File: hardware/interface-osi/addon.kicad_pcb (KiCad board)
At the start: 2 copper layers, 43.2 x 54 mm, 23 parts, among them J1 Conn_01x16, U1 4066, U2 74HC14

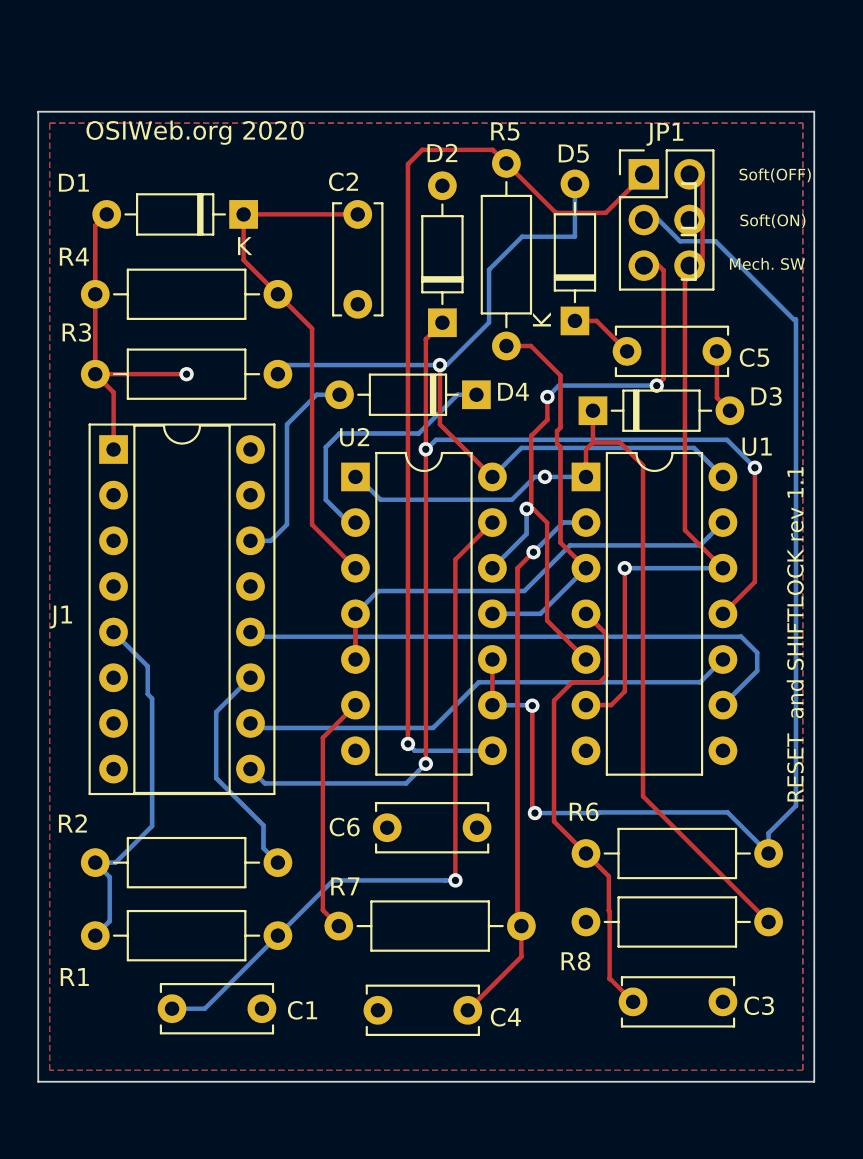
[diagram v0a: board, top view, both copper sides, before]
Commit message: OSI reset/shiftlock addon- add  mounting holes
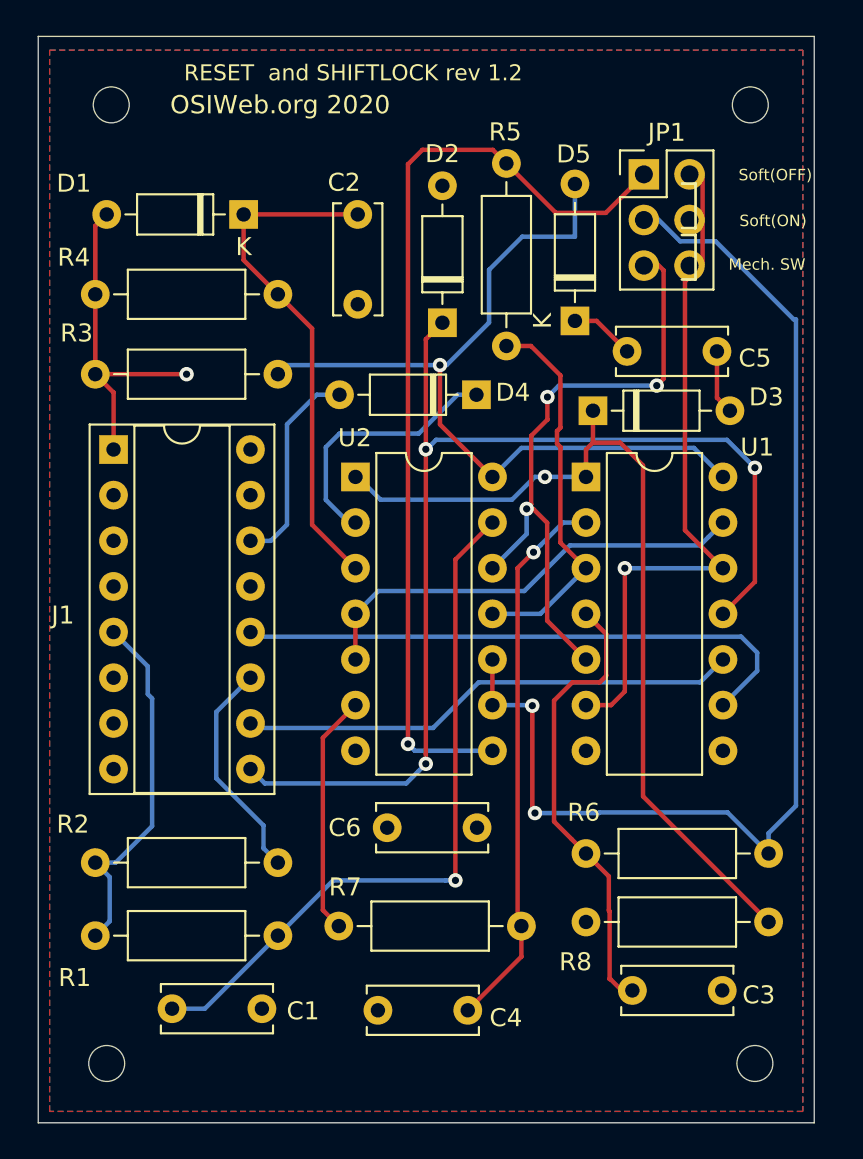
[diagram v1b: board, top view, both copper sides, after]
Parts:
- added REF**: MountingHole_2mm, MountingHole:MountingHole_2mm, F.Cu at (110.7, 42.2)
- added REF**: MountingHole_2mm, MountingHole:MountingHole_2mm, F.Cu at (110.5, 95.5)
- added REF**: MountingHole_2mm, MountingHole:MountingHole_2mm, F.Cu at (146.3, 42.2)
- added REF**: MountingHole_2mm, MountingHole:MountingHole_2mm, F.Cu at (146.6, 95.5)
- moved C3 0.64 mm to (144.7, 91.4)
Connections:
- net ~RESET renamed ~{RESET}
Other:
- board size 43.2 x 54 mm -> 43.2 x 60.5 mm
- net class Default removed
- board text added: "RESET and SHIFTLOCK rev 1.2"
- board text removed: "RESET and SHIFTLOCK rev 1.1"

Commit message: Clean up DRC errors
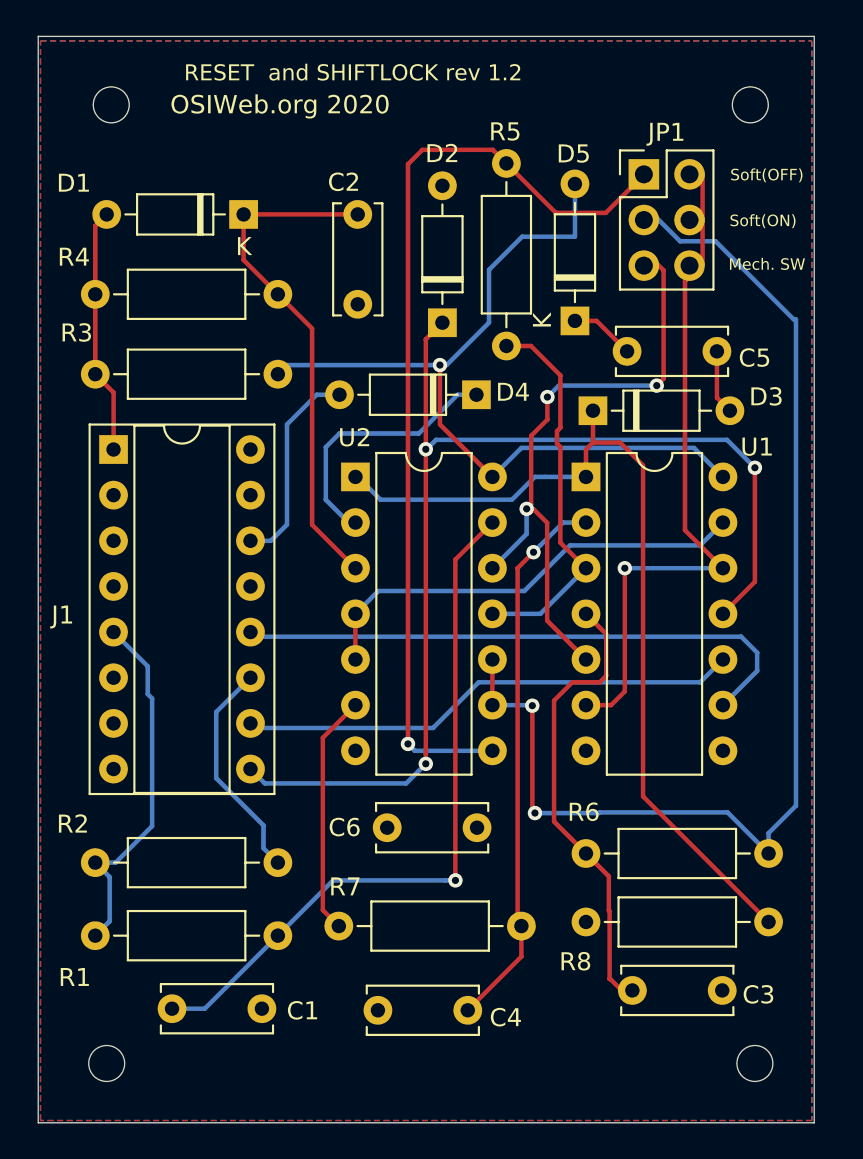
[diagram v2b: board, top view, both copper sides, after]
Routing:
- net /Break1: track 18.8 -> 13.8 mm, vias 1 -> 0
- net Net-(C3-Pad2): track 26.6 -> 26.0 mm
- net Net-(D3-Pad1): vias 1 -> 0
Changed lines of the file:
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@@
     (pad "" np_thru_hole circle (at 0 0) (size 2 2) (drill 2) (layers *.Cu *.Mask))
   )
-  (gr_line (start 142.494 49.403) (end 143.256 49.403) (layer "F.SilkS") (width 0.15))
-  (gr_line (start 142.494 49.022) (end 143.256 49.022) (layer "F.SilkS") (width 0.15))
-  (gr_line (start 142.494 46.5455) (end 143.256 46.5455) (layer "F.SilkS") (width 0.15))
-  (gr_line (start 143.256 49.022) (end 143.256 46.5455) (layer "F.SilkS") (width 0.15))
-  (gr_line (start 142.494 51.8795) (end 143.256 51.8795) (layer "F.SilkS") (width 0.15))
-  (gr_line (start 143.256 51.8795) (end 143.256 49.403) (layer "F.SilkS") (width 0.15))
   (gr_rect (start 149.86 98.806) (end 106.68 38.354) (layer "Edge.Cuts") (width 0.0508) (fill none))
-  (gr_text "Soft(ON)" (at 147.56892 48.6156) (layer "F.SilkS")
+  (gr_text "Soft(ON)" (at 147.016893 48.6156) (layer "F.SilkS")
     (effects (font (size 0.635 0.635) (thickness 0.127)))
   )
-  (gr_text "Soft(OFF)" (at 147.69592 46.06544) (layer "F.SilkS")
+  (gr_text "Soft(OFF)" (at 147.22856 46.06544) (layer "F.SilkS")
     (effects (font (size 0.635 0.635) (thickness 0.127)))
   )
@@
   (segment (start 110.871 58.166) (end 109.855 57.15) (width 0.25) (layer "F.Cu") (net 2))
   (segment (start 109.855 52.705) (end 109.855 48.895) (width 0.25) (layer "F.Cu") (net 2))
-  (segment (start 109.855 57.15) (end 114.935 57.15) (width 0.25) (layer "F.Cu") (net 2))
   (segment (start 110.871 61.341) (end 110.871 58.166) (width 0.25) (layer "F.Cu") (net 2))
   (segment (start 109.855 48.895) (end 110.49 48.26) (width 0.25) (layer "F.Cu") (net 2))
-  (via (at 114.935 57.15) (size 0.8) (drill 0.4) (layers "F.Cu" "B.Cu") (net 2))
   (segment (start 128.246598 61.327758) (end 128.246598 78.264325) (width 0.25) (layer "F.Cu") (net 3))
   (segment (start 128.246598 78.264325) (end 128.246598 78.83001) (width 0.25) (layer "F.Cu") (net 3))
@@
   (segment (start 148.844 54.102) (end 148.717 54.102) (width 0.25) (layer "B.Cu") (net 4))
   (segment (start 147.32 83.82) (end 147.32 82.68863) (width 0.25) (layer "B.Cu") (net 4))
-  (segment (start 147.32 83.82) (end 147.2565 83.7565) (width 0.25) (layer "B.Cu") (net 4))
   (segment (start 137.922 81.534) (end 145.034 81.534) (width 0.25) (layer "B.Cu") (net 4))
   (segment (start 142.39748 49.75352) (end 141.10716 48.4632) (width 0.25) (layer "B.Cu") (net 4))
@@
   (segment (start 138.285001 73.931999) (end 137.922 74.295) (width 0.25) (layer "F.Cu") (net 16))
   (segment (start 136.360001 83.020001) (end 137.16 83.82) (width 0.25) (layer "F.Cu") (net 16))
-  (segment (start 137.16 83.82) (end 137.795 83.82) (width 0.25) (layer "F.Cu") (net 16))
   (segment (start 138.285001 71.610001) (end 138.285001 73.931999) (width 0.25) (layer "F.Cu") (net 16))
   (segment (start 136.398 74.295) (end 135.382 75.311) (width 0.25) (layer "F.Cu") (net 16))
@@
   (segment (start 139.065 60.96) (end 137.541 60.96) (width 0.25) (layer "F.Cu") (net 22))
   (segment (start 140.335 62.23) (end 139.065 60.96) (width 0.25) (layer "F.Cu") (net 22))
-  (via (at 134.874 62.865) (size 0.8) (drill 0.4) (layers "F.Cu" "B.Cu") (net 22))
   (segment (start 125.73 64.135) (end 133.038315 64.135) (width 0.25) (layer "B.Cu") (net 22))
   (segment (start 133.038315 64.135) (end 134.308315 62.865) (width 0.25) (layer "B.Cu") (net 22))
@@
   (segment (start 128.0541 44.6659) (end 127.254 45.466) (width 0.25) (layer "F.Cu") (net 24))
   (segment (start 138.26236 48.17364) (end 135.4836 48.17364) (width 0.25) (layer "F.Cu") (net 24))
-  (segment (start 141.10716 45.9232) (end 140.90904 45.9232) (width 0.25) (layer "F.Cu") (net 24))
   (segment (start 131.97586 44.6659) (end 128.0541 44.6659) (width 0.25) (layer "F.Cu") (net 24))
   (segment (start 140.38072 46.05528) (end 138.26236 48.17364) (width 0.25) (layer "F.Cu") (net 24))
@@
     (polygon
       (pts
-        (xy 149.225 98.171)
-        (xy 107.315 98.171)
-        (xy 107.315 39.116)
-        (xy 149.225 39.116)
+        (xy 149.733 98.679)
+        (xy 106.807 98.679)
+        (xy 106.807 38.608)
+        (xy 149.733 38.608)
       )
     )
@@
     (polygon
       (pts
-        (xy 149.225 98.171)
-        (xy 107.315 98.171)
-        (xy 107.315 39.116)
-        (xy 149.225 39.116)
+        (xy 149.733 98.679)
+        (xy 106.807 98.679)
+        (xy 106.807 38.608)
+        (xy 149.733 38.608)
       )
     )

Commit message: Cleanup RESET+SHIFTLOCK addon
- replaced DIP header with 13-pin 0.1" vertical header.  Added labels to
the pins.

- removed left over unused diode

- reversed default on / default off labels on shiftlock mode jumper
block.
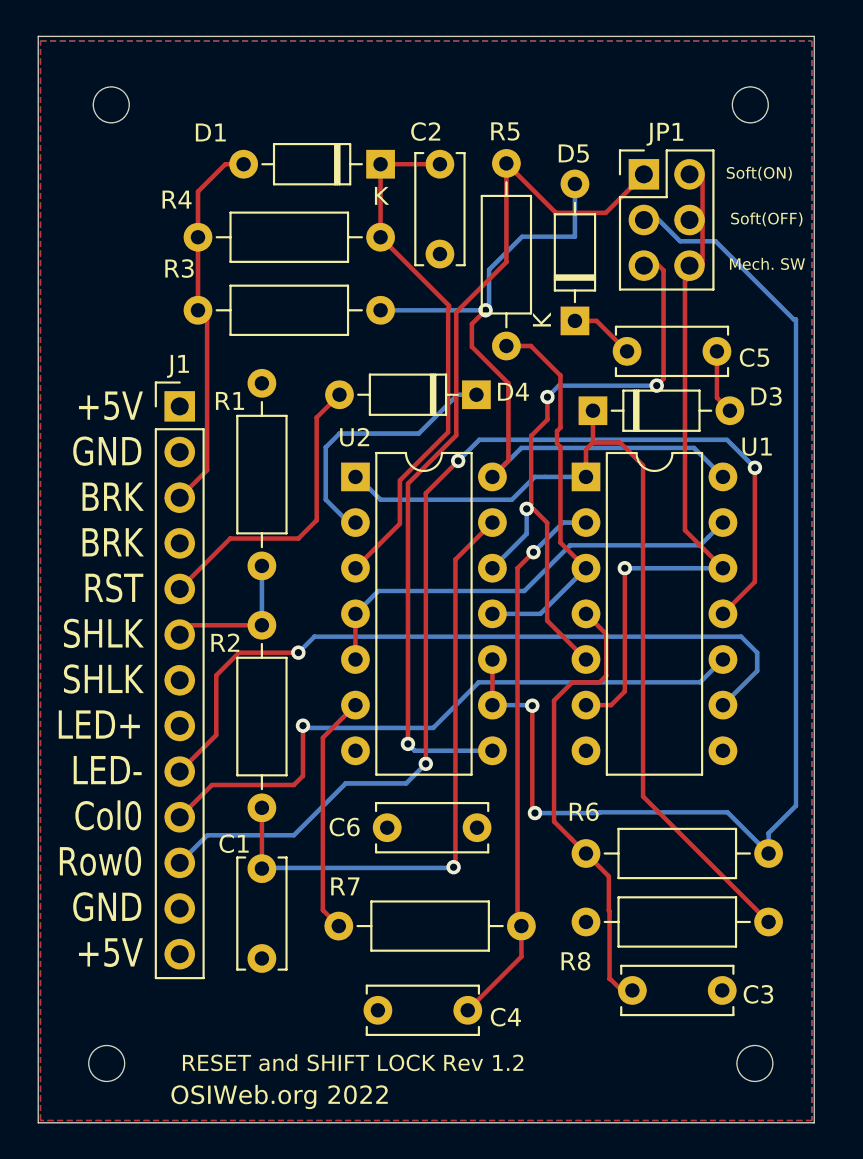
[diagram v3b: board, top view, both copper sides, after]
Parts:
- removed D2: 1N914, Diode_THT:D_DO-35_SOD27_P7.62mm_Horizontal
- J1: value Conn_01x16 -> Conn_01x13_Male; footprint Package_DIP:DIP-16_W7.62mm_Socket -> Connector_PinHeader_2.54mm:PinHeader_1x13_P2.54mm_Vertical
- moved R1 26.7 mm to (119.1, 57.7), turned to -90 degrees
- moved R2 19.6 mm to (119.1, 71.1), turned to -90 degrees
- moved D1 8.12 mm to (125.7, 45.5)
- moved R3 6.73 mm to (125.7, 53.6)
- moved R4 6.54 mm to (115.6, 49.5)
- moved C2 5.36 mm to (129.0, 45.5)
- moved J1 4.39 mm to (114.6, 58.9)
- moved C1 2.79 mm to (119.1, 89.7), turned to 90 degrees
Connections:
- J1 pad 1: /Break1 -> ShifLockLED+
- J1 pad 11: ShifLockLED+ -> Row0
- J1 pad 12: ShiftLockLED- -> GND
- J1 pad 13: Net-(J1-Pad13) -> ShifLockLED+
- J1 pad 2: Net-(J1-Pad2) -> GND
- J1 pad 3: GND -> /Break1
- J1 pad 4: Net-(J1-Pad4) -> GND
- J1 pad 5: /ShiftLock1 -> ~{RESET}
- J1 pad 6: Net-(J1-Pad6) -> /ShiftLock1
- J1 pad 8: GND -> ShifLockLED+
- J1 pad 9: Row0 -> ShiftLockLED-
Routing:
- net ShifLockLED+: track 58.4 -> 41.6 mm
- net /ShiftLock1: track 20.4 -> 8.09 mm
- net ShiftLockLED-: track 32.4 -> 41.3 mm, vias 0 -> 1
- net Col0: track 28.0 -> 35.7 mm, vias 0 -> 1
- net /Break1: track 13.8 -> 21.0 mm
- net Net-(C1-Pad2): track 39.5 -> 34.2 mm
- net ~{RESET}: track 11.6 -> 16.7 mm
- net Net-(JP1-Pad1): track 52.9 -> 49.1 mm
- net Row0: track 63.5 -> 60.1 mm
- net Net-(C2-Pad1): track 28.6 -> 29.5 mm
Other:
- board text added: "${COMPANY} 2022"
- board text added: "${TITLE} Rev ${REVISION}"
- board text added: "+5V GND BRK BRK RST SHLK SHLK LED+ LED- Col0 Row0 GND +5V"
- board text removed: "OSIWeb.org 2020"
- board text removed: "RESET and SHIFTLOCK rev 1.2"
